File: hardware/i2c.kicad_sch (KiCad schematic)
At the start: 18 parts, among them J1 INPUT USB, U1 TPS259261, U2 AP2125N-3.3TRG1

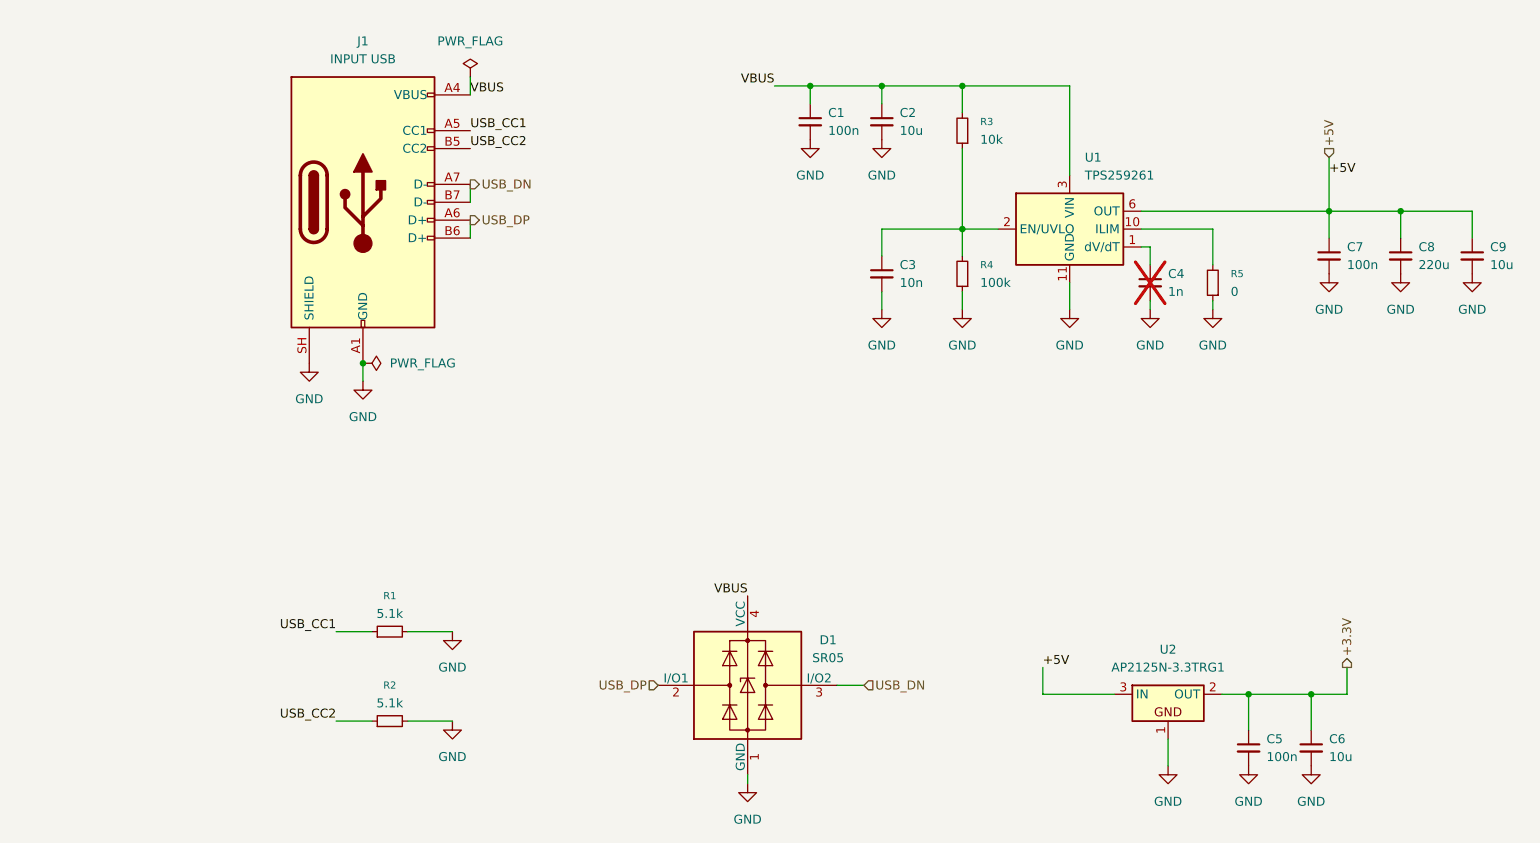
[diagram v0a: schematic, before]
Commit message: separate left/right part design, schematic
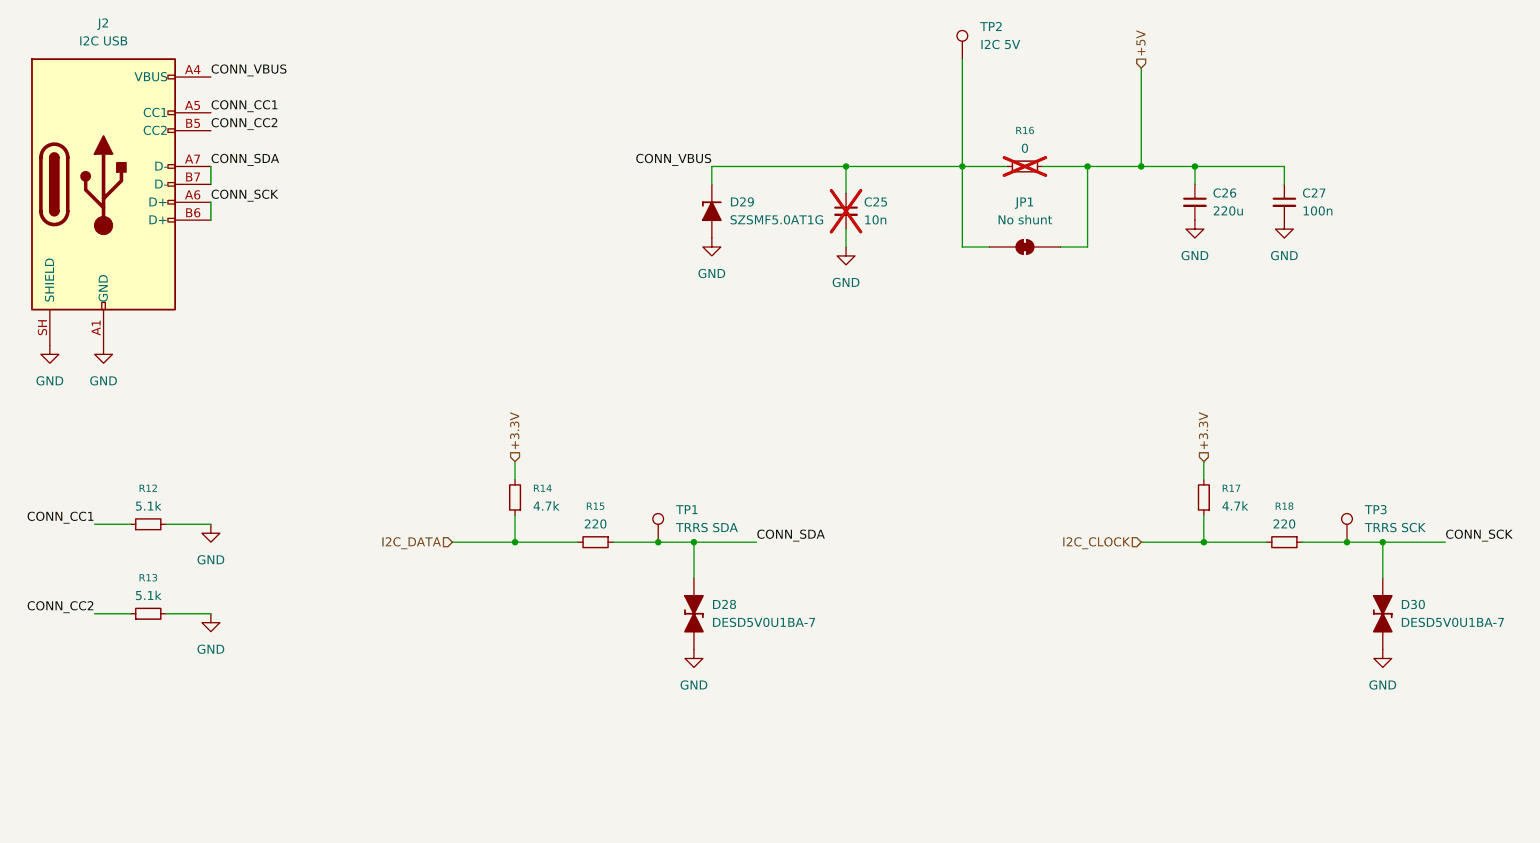
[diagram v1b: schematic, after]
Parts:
- removed C1, C5, C7: 100n, PCM_Capacitor_SMD_AKL:C_0603_1608Metric_Pad1.05x0.95mm_HandSolder, symbol Device:C_Small
- removed C2: 10u, PCM_Capacitor_SMD_AKL:C_0603_1608Metric_Pad1.05x0.95mm_HandSolder, symbol Device:C_Small
- removed C3: 10n, PCM_Capacitor_SMD_AKL:C_0603_1608Metric_Pad1.05x0.95mm_HandSolder, symbol Device:C_Small
- removed C4: 1n, PCM_Capacitor_SMD_AKL:C_0603_1608Metric_Pad1.05x0.95mm_HandSolder, symbol Device:C_Small
- removed C6, C9: 10u, PCM_Capacitor_SMD_AKL:C_0805_2012Metric_Pad1.15x1.40mm_HandSolder, symbol Device:C_Small
- removed C8: 220u, PCM_Capacitor_SMD_AKL:C_1210_3225Metric_Pad1.33x2.70mm_HandSolder, symbol Device:C_Small
- removed D1: SR05, Package_TO_SOT_SMD:SOT-143, symbol Power_Protection:PRTR5V0U2X
- removed J1: INPUT USB, Connector_USB:USB_C_Receptacle_GCT_USB4105-xx-A_16P_TopMnt_Horizontal, symbol Connector:USB_C_Receptacle_USB2.0_14P
- removed R1, R2: 5.1k, PCM_Resistor_SMD_AKL:R_0603_1608Metric_Pad0.98x0.95mm_HandSolder, symbol Device:R_Small
- removed R3: 10k, PCM_Resistor_SMD_AKL:R_0603_1608Metric, symbol Device:R_Small
- removed R4: 100k, PCM_Resistor_SMD_AKL:R_0603_1608Metric, symbol Device:R_Small
- removed R5: 0, PCM_Resistor_SMD_AKL:R_0603_1608Metric_Pad0.98x0.95mm_HandSolder, symbol Device:R_Small
- removed U1: TPS259261, Package_SON:VSON-10-1EP_3x3mm_P0.5mm_EP1.65x2.4mm_ThermalVias, symbol Power_Management:TPS2592xx
- removed U2: AP2125N-3.3TRG1, PCM_Package_TO_SOT_SMD_AKL:SOT-23, symbol PCM_Voltage_Regulator_AKL:AP2125N-3.3TRG1
- added C25: 10n, PCM_Capacitor_SMD_AKL:C_0603_1608Metric_Pad1.05x0.95mm_HandSolder, symbol Device:C_Small
- added C26: 220u, PCM_Capacitor_SMD_AKL:C_1210_3225Metric_Pad1.33x2.70mm_HandSolder, symbol Device:C_Small
- added C27: 100n, PCM_Capacitor_SMD_AKL:C_0603_1608Metric, symbol Device:C_Small
- added D28, D30: DESD5V0U1BA-7, PCM_Diode_SMD_AKL:D_SOD-323_HandSoldering, symbol PCM_Diode_TVS_AKL:D_TVS_Bidirectional_Generic
- added D29: SZSMF5.0AT1G, PCM_Diode_SMD_Handsoldering_AKL:D_SOD-123_TVS, symbol PCM_Diode_TVS_AKL:D_TVS_Unidirectional_Generic
- added J2: I2C USB, Connector_USB:USB_C_Receptacle_GCT_USB4105-xx-A_16P_TopMnt_Horizontal, symbol Connector:USB_C_Receptacle_USB2.0_14P
- added JP1: No shunt, Jumper:SolderJumper-2_P1.3mm_Bridged_RoundedPad1.0x1.5mm, symbol Jumper:SolderJumper_2_Bridged
- added R12, R13: 5.1k, PCM_Resistor_SMD_AKL:R_0603_1608Metric_Pad0.98x0.95mm_HandSolder, symbol Device:R_Small
- added R14, R17: 4.7k, PCM_Resistor_SMD_AKL:R_0603_1608Metric_Pad0.98x0.95mm_HandSolder, symbol Device:R_Small
- added R15, R18: 220, PCM_Resistor_SMD_AKL:R_0603_1608Metric_Pad0.98x0.95mm_HandSolder, symbol Device:R_Small
- added R16: 0, PCM_Resistor_SMD_AKL:R_1206_3216Metric_Pad1.30x1.75mm_HandSolder, symbol Device:R_Small
- added TP1: TRRS SDA, TestPoint:TestPoint_Pad_D2.0mm, symbol Connector:TestPoint
- added TP2: I2C 5V, TestPoint:TestPoint_Pad_D2.0mm, symbol Connector:TestPoint
- added TP3: TRRS SCK, TestPoint:TestPoint_Pad_D2.0mm, symbol Connector:TestPoint
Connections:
- net +3.3V: now also R14.2, R17.2
- net +5V: now also C26.1, C27.1, JP1.2 (B), R16.1
- net GND: now also C25.2, C26.2, C27.2, D28.1 (K), D29.2 (A), D30.1 (K), J2.A1 (GND), J2.A12 (GND), J2.B1 (GND), J2.B12 (GND), J2.SH (SHIELD), R12.2, R13.2
- new net CONN_CC1: J2.A5 (CC1), R12.1
- new net CONN_CC2: J2.B5 (CC2), R13.1
- new net CONN_SCK: D30.2 (A), J2.A6 (D+), J2.B6 (D+), R18.1, TP3.1
- new net CONN_SDA: D28.2 (A), J2.A7 (D-), J2.B7 (D-), R15.1, TP1.1
- new net CONN_VBUS: C25.1, D29.1 (K), J2.A4 (VBUS), J2.A9 (VBUS), J2.B4 (VBUS), J2.B9 (VBUS), JP1.1 (A), R16.2, TP2.1
- new net I2C_CLOCK: R17.1, R18.2
- new net I2C_DATA: R14.1, R15.2
